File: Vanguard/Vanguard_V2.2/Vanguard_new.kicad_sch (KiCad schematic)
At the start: 78 parts, among them J1 USB_C_Receptacle_USB2.0_16P, J2 Conn_02x03_Pin, J3 Micro_SD_Card_Det1, J4 STARBOARD_SERVO, J5 PORTSIDE_SERVO, J6 Conn_01x02_Pin, J7 EJECTION_SERVO, Q1 BSS138, Q2 BSS138, Q3 BSS138, Q4 BSS138, U1 ATSAMD11D14A-M, U2 ATmega4809-A, U3 AT25DF641A-SH-T, U4 AP2112K-3.3, U5 BD1020HFV, U6 BNO086, U7 TXB0104D, U8 TPS61092, U9 MPM3610AGQV-P, Y1 32.768kHz

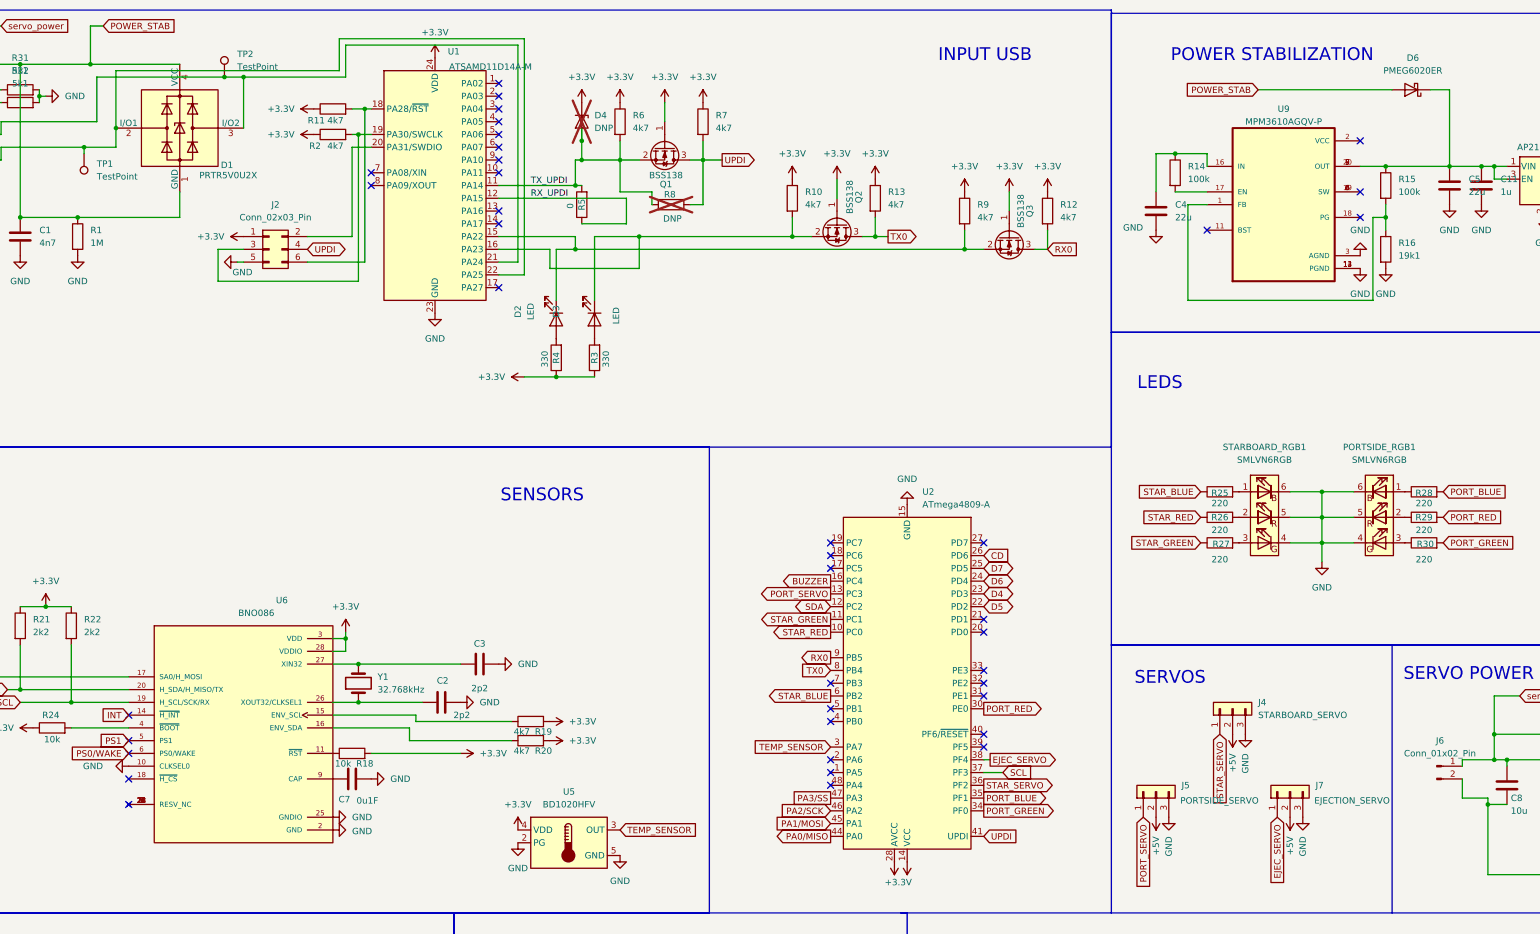
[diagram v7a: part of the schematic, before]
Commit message: an input label to U9 and MC label moved a bit
Added a label in the input pin from U9 from the VBUS of USB. Moved the SPI pins and temperature sensor pins in the MC. @stygmatic have a look and ask me questions if needed
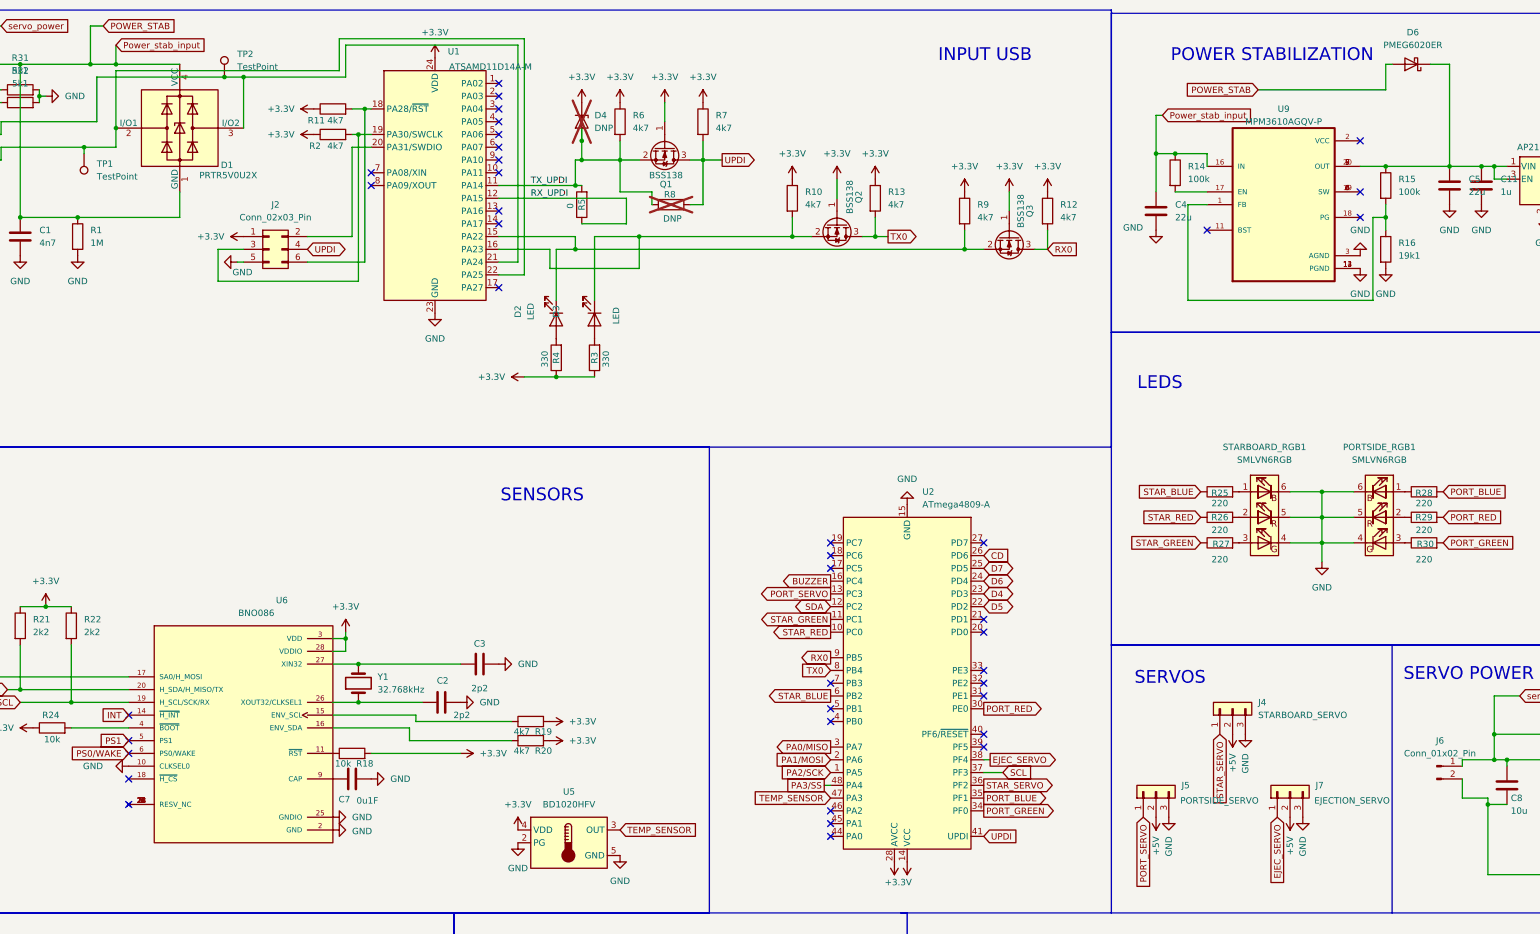
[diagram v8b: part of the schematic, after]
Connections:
- net PA0/MISO: now also U2.3 (PA7); no longer U2.44 (PA0)
- net PA1/MOSI: now also U2.2 (PA6); no longer U2.45 (PA1)
- net PA2/SCK: now also U2.1 (PA5); no longer U2.46 (PA2)
- net PA3/SS: now also U2.48 (PA4); no longer U2.47 (PA3)
- net POWER_STAB: now also C4.1, R14.1, U9.16 (IN)
- net TEMP_SENSOR: now also U2.47 (PA3); no longer U2.3 (PA7)
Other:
- moved on the sheet: D6
